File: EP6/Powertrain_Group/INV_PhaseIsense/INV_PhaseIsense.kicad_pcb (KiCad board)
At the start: 4 copper layers, 148 x 29 mm, 4 parts, among them IC1 LZSR_80-TP, IC2 LZSR_80-TP, IC3 LZSR_80-TP, J1 to INV_Mainboard_TI

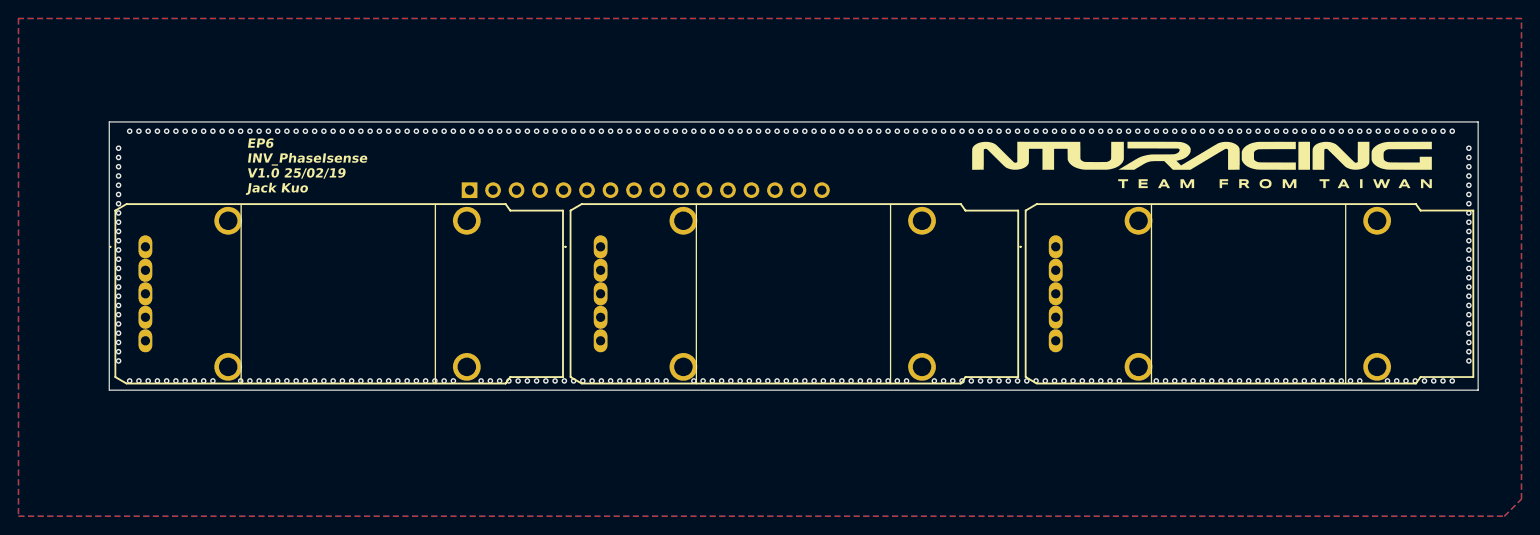
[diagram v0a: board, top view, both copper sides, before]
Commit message: update INV_PhaseIsense to V1.1
offset connector to mainboard by 6 mm to better match power module
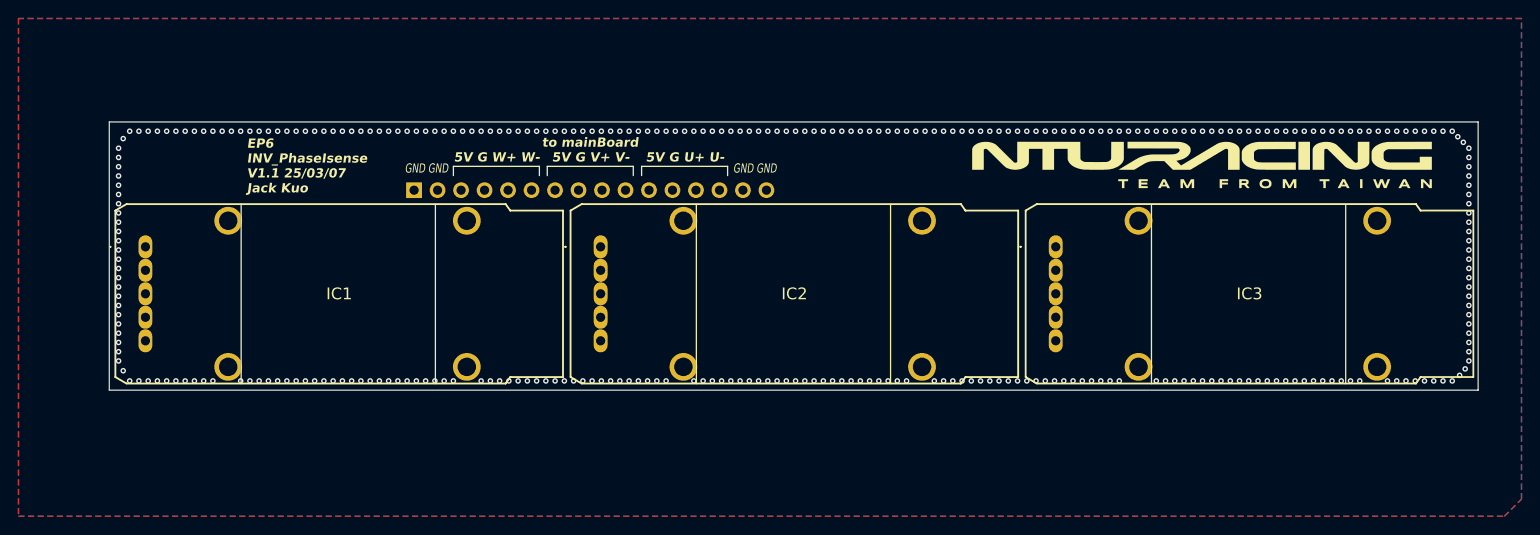
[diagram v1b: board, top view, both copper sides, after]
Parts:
- IC1, IC2, IC3: value LZSR_80-TP -> LZSR_80-P
- moved J1 6.00 mm to (105.0, 46.4)
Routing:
- net /U+: track 44.9 -> 51.0 mm
- net /U-: track 44.3 -> 50.1 mm
- net /U_PWR: track 50.0 -> 55.8 mm
- net /U_GND: track 49.2 -> 55.0 mm
- net /V_PWR: track 9.95 -> 14.4 mm
- net /V_GND: track 10.6 -> 15.0 mm
- net /W_GND: track 48.4 -> 45.2 mm
- net /W-: track 55.6 -> 53.1 mm
- net /W+: track 55.0 -> 52.5 mm
- net /W_PWR: track 47.8 -> 45.9 mm
- net /V-: track 18.9 -> 17.9 mm
- net GND: vias 323 -> 329
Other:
- board text added: "5V G U+ U-"
- board text added: "5V G V+ V-"
- board text added: "5V G W+ W-"
- board text added: "EP6 INV_PhaseIsense V1.1 25/03/07 Jack Kuo"
- board text added: "GND GND"
- board text added: "to mainBoard"
- board text removed: "EP6 INV_PhaseIsense V1.0 25/02/19 Jack Kuo"

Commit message: update INV_PhaseIsense to V1.2
V1.2
shift connector up about 6mm and right 6mm exactly (back to where V1.0 is)
for better bus assembly
add mounting hole for more sturdy mounting
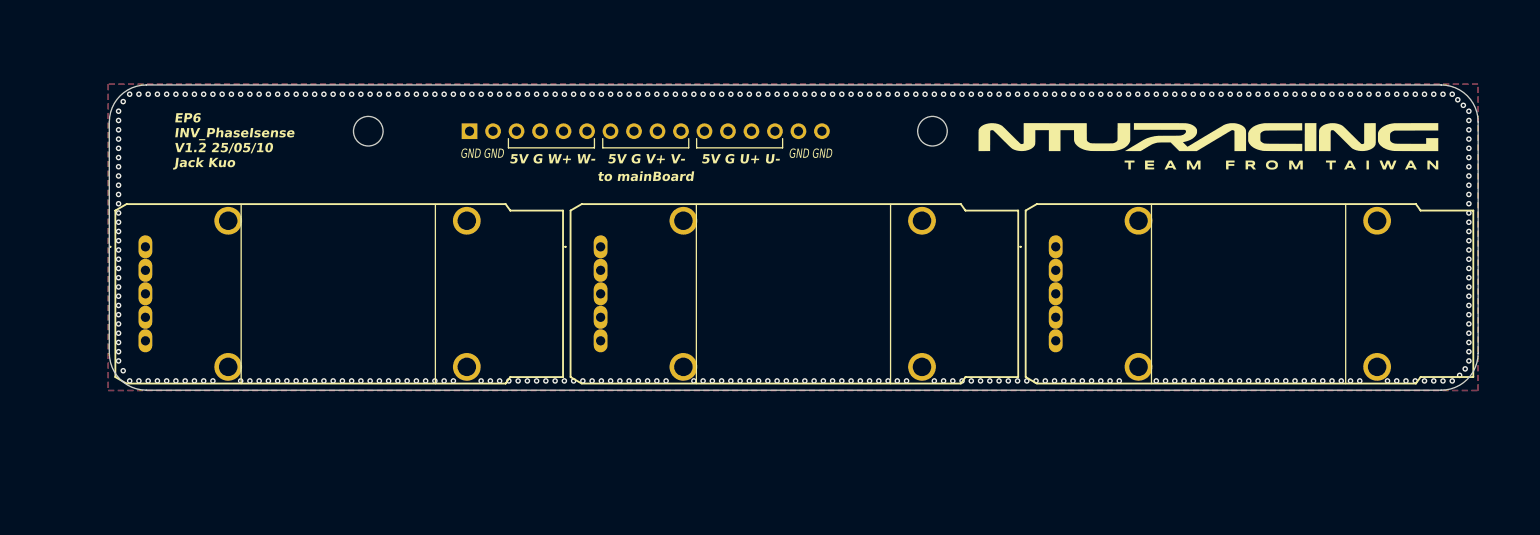
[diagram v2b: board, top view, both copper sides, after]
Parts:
- added H1: MountingHole, MountingHole:MountingHole_3.2mm_M3, F.Cu at (100.0, 40.0)
- added H2: MountingHole, MountingHole:MountingHole_3.2mm_M3, F.Cu at (161.0, 40.0)
- moved J1 8.75 mm to (111.0, 40.0)
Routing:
- net /W_GND: track 45.2 -> 54.2 mm
- net /W-: track 53.1 -> 60.8 mm
- net /W+: track 52.5 -> 60.1 mm
- net /W_PWR: track 45.9 -> 53.6 mm
- net /V-: track 17.9 -> 24.6 mm
- net /V+: track 17.2 -> 23.9 mm
- net /U-: track 50.1 -> 55.9 mm
- net /U+: track 51.0 -> 55.1 mm
- net /U_PWR: track 55.8 -> 52.9 mm
- net /V_GND: track 15.0 -> 17.0 mm
- net /V_PWR: track 14.4 -> 16.3 mm
- net /U_GND: track 55.0 -> 53.4 mm
- net GND: vias 329 -> 337
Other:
- board size 148 x 29 mm -> 148 x 33 mm
- board text added: "EP6 INV_PhaseIsense V1.2 25/05/10 Jack Kuo"
- board text removed: "EP6 INV_PhaseIsense V1.1 25/03/07 Jack Kuo"
